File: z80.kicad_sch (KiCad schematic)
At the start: 46 parts, among them IC4 Z80CPU, IC5 LC3664, IC901 TL974

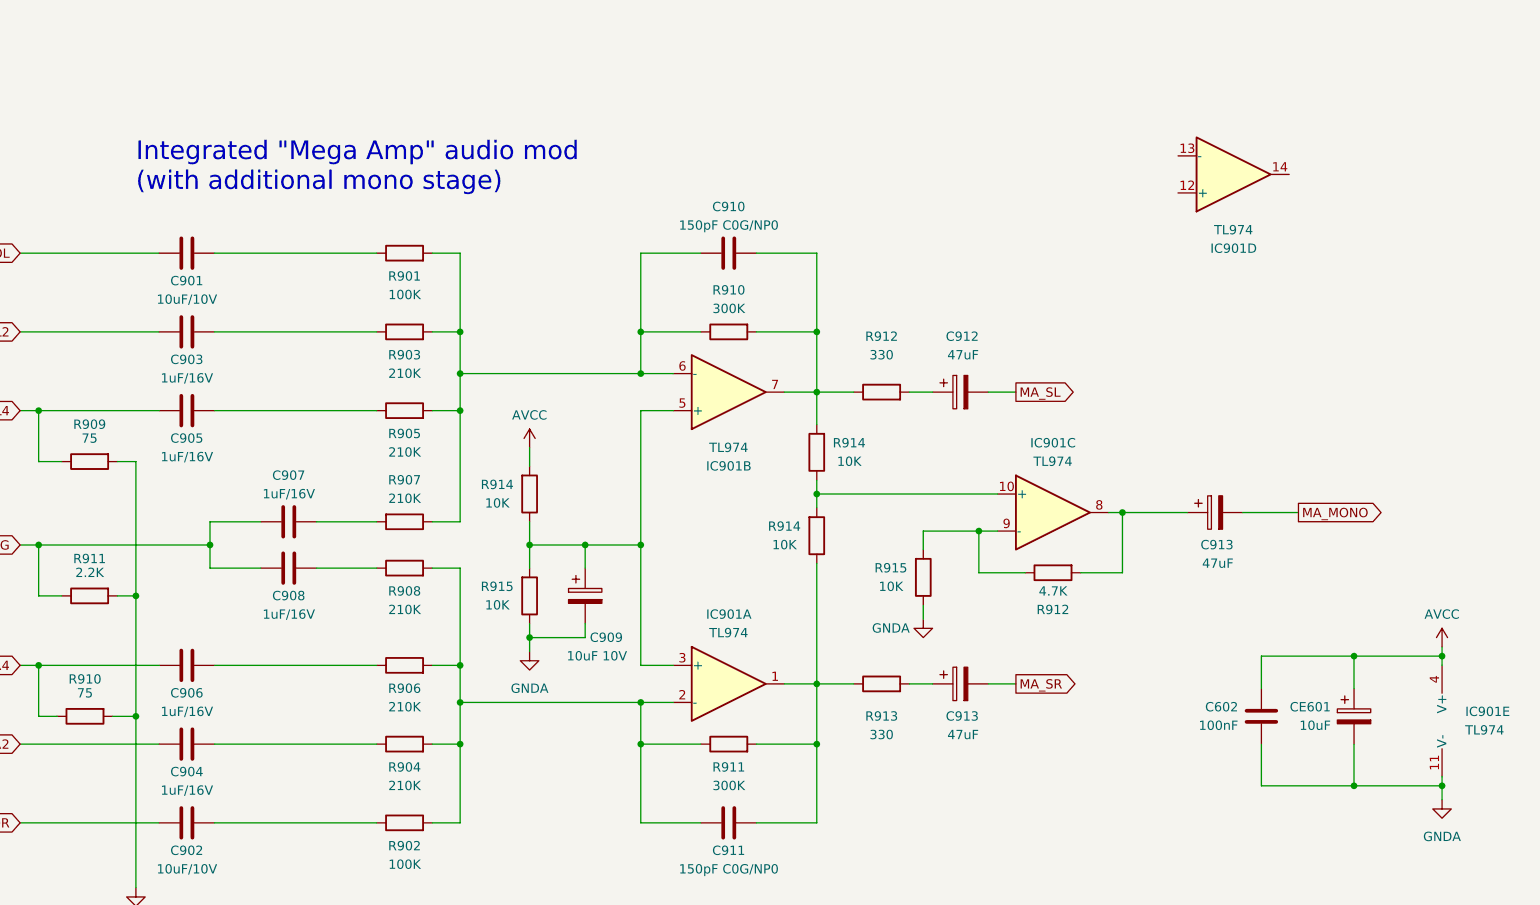
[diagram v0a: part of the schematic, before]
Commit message: Remove mono audio, switch to 2-unit opamp.
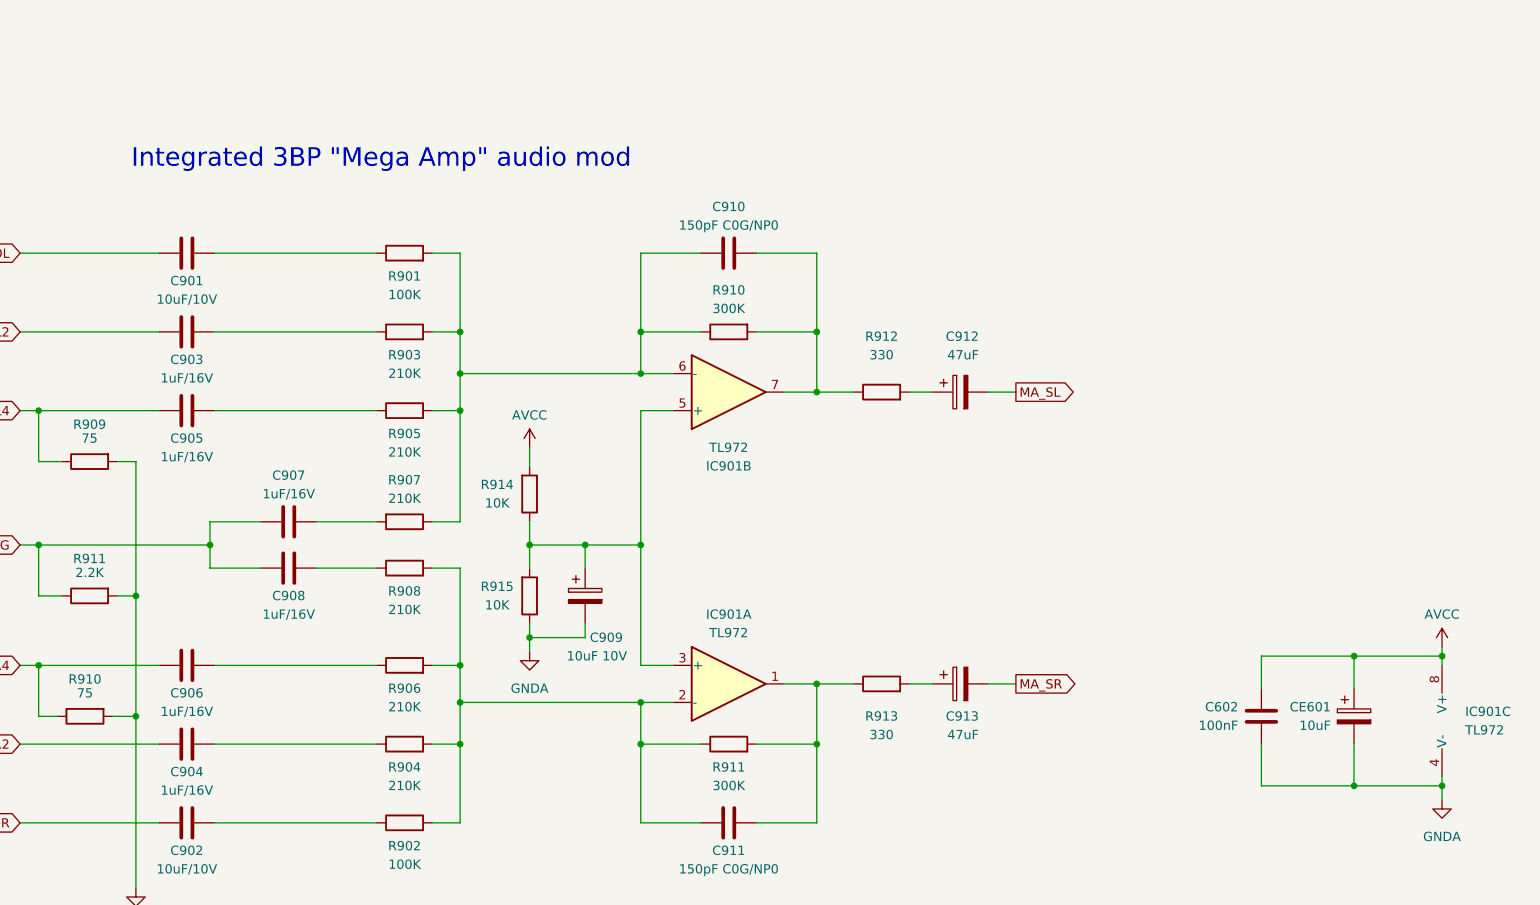
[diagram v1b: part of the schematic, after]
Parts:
- removed C913: 47uF, Capacitor_THT:CP_Radial_D5.0mm_P2.50mm, symbol Device:C_Polarized
- removed unit 4 of IC901
- removed unit 3 of IC901
- removed R912: 4.7K, Resistor_SMD:R_0805_2012Metric, symbol Device:R
- removed R914 (x2), R915: 10K, Resistor_SMD:R_0805_2012Metric, symbol Device:R
- IC901: value TL974 -> TL972; footprint Package_SO:SO-14_3.9x8.65mm_P1.27mm -> Package_SO:SO-8_3.9x4.9mm_P1.27mm; symbol Amplifier_Operational:TL064 -> Amplifier_Operational:TL062
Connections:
- net AVCC: now also IC901.8 (V+); no longer IC901.4 (V+)
- net GNDA: now also IC901.4 (V-); no longer IC901.11 (V-)
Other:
- note added: "Integrated 3BP "Mega Amp" audio mod"
- note removed: "Integrated "Mega Amp" audio mod (with additional mono stage)"

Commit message: Added LCSC Part # for some of the bird seed
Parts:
- C602: LCSC Part # (none) -> C2237864
- C901, C902: LCSC Part # (none) -> C2265547
- C903: LCSC Part # (none) -> C2224419
- C903, C904, C905, C906, C907, C908: LCSC Part # (none) -> C1850591
- C910, C911: LCSC Part # (none) -> C2230620
- R901, R902: LCSC Part # (none) -> C844935
- R903, R904, R905, R906, R907, R908: LCSC Part # (none) -> C2080690
- R909, R910: LCSC Part # (none) -> C313959
- R910, R911: LCSC Part # (none) -> C1881308
- R911: LCSC Part # (none) -> C3008897
- R912, R913: LCSC Part # (none) -> C844839
- R914, R915: LCSC Part # (none) -> C844937
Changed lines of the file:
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@@
+      (effects (font (size 1.27 1.27)) hide)
+    )
+    (property "LCSC Part #" "C1850591" (at 115.57 231.775 0)
       (effects (font (size 1.27 1.27)) hide)
     )
@@
       (effects (font (size 1.27 1.27)) hide)
     )
+    (property "LCSC Part #" "C2230620" (at 189.865 175.26 0)
+      (effects (font (size 1.27 1.27)) hide)
+    )
     (pin "1")
     (pin "2")
@@
       (effects (font (size 1.27 1.27)) hide)
     )
+    (property "LCSC Part #" "C2265547" (at 115.57 253.365 0)
+      (effects (font (size 1.27 1.27)) hide)
+    )
     (pin "1")
     (pin "2")
@@
     )
     (property "DigiKey" "P210KCCT-ND" (at 145.415 186.055 0)
+      (effects (font (size 1.27 1.27)) hide)
+    )
+    (property "LCSC Part #" "C2080690" (at 145.415 186.055 0)
       (effects (font (size 1.27 1.27)) hide)
     )
@@
     )
     (property "DigiKey" "493-13447-1-ND" (at 221.615 234.315 0)
+      (effects (font (size 1.27 1.27)) hide)
+    )
+    (property "LCSC Part #" "" (at 221.615 234.315 0)
       (effects (font (size 1.27 1.27)) hide)
     )
@@
     )
     (property "DigiKey" "296-21693-1-ND" (at 189.865 234.315 0)
+      (effects (font (size 1.27 1.27)) hide)
+    )
+    (property "LCSC Part #" "" (at 189.865 234.315 0)
       (effects (font (size 1.27 1.27)) hide)
     )
@@
       (effects (font (size 1.27 1.27)) hide)
     )
+    (property "LCSC Part #" "C2080690" (at 145.415 212.09 0)
+      (effects (font (size 1.27 1.27)) hide)
+    )
     (pin "1")
     (pin "2")
@@
       (effects (font (size 1.27 1.27)) hide)
     )
+    (property "LCSC Part #" "C313959" (at 101.6 238.76 0)
+      (effects (font (size 1.27 1.27)) hide)
+    )
     (pin "1")
     (pin "2")
@@
     )
     (property "DigiKey" "" (at 115.57 242.57 0)
+      (effects (font (size 1.27 1.27)) hide)
+    )
+    (property "LCSC Part #" "C1850591" (at 115.57 242.57 0)
       (effects (font (size 1.27 1.27)) hide)
     )
@@
       (effects (font (size 1.27 1.27)) hide)
     )
+    (property "LCSC Part #" "C2080690" (at 145.415 231.775 0)
+      (effects (font (size 1.27 1.27)) hide)
+    )
     (pin "1")
     (pin "2")
@@
     )
     (property "DigiKey" "P210KCCT-ND" (at 145.415 242.57 0)
+      (effects (font (size 1.27 1.27)) hide)
+    )
+    (property "LCSC Part #" "C2080690" (at 145.415 242.57 0)
       (effects (font (size 1.27 1.27)) hide)
     )
@@
       (effects (font (size 1.27 1.27)) hide)
     )
+    (property "LCSC Part #" "C2237864" (at 262.89 238.76 0)
+      (effects (font (size 1.27 1.27)) hide)
+    )
     (pin "1")
     (pin "2")
@@
     )
     (property "DigiKey" "" (at 145.415 175.26 0)
+      (effects (font (size 1.27 1.27)) hide)
+    )
+    (property "LCSC Part #" "C844935" (at 145.415 175.26 0)
       (effects (font (size 1.27 1.27)) hide)
     )
@@
       (effects (font (size 1.27 1.27)) hide)
     )
+    (property "LCSC Part #" "C313959" (at 52.07 175.26 0)
+      (effects (font (size 1.27 1.27)) hide)
+    )
     (pin "1")
     (pin "2")
@@
     )
     (property "DigiKey" "296-21693-1-ND" (at 189.865 194.31 0)
+      (effects (font (size 1.27 1.27)) hide)
+    )
+    (property "LCSC Part #" "" (at 189.865 194.31 0)
       (effects (font (size 1.27 1.27)) hide)
     )
@@
       (effects (font (size 1.27 1.27)) hide)
     )
+    (property "LCSC Part #" "" (at 80.772 33.782 0)
+      (effects (font (size 1.27 1.27)) hide)
+    )
     (pin "1")
     (pin "2")
@@
       (effects (font (size 1.27 1.27)) hide)
     )
+    (property "LCSC Part #" "C2080690" (at 145.415 218.44 0)
+      (effects (font (size 1.27 1.27)) hide)
+    )
     (pin "1")
     (pin "2")
@@
       (effects (font (size 1.27 1.27)) hide)
     )
+    (property "LCSC Part #" "C2224419" (at 167.64 33.655 0)
+      (effects (font (size 1.27 1.27)) hide)
+    )
     (pin "1")
     (pin "2")
@@
       (effects (font (size 1.27 1.27)) hide)
     )
+    (property "LCSC Part #" "C2265547" (at 115.57 175.26 0)
+      (effects (font (size 1.27 1.27)) hide)
+    )
     (pin "1")
     (pin "2")
@@
       (effects (font (size 1.27 1.27)) hide)
     )
+    (property "LCSC Part #" "C844937" (at 162.56 222.25 0)
+      (effects (font (size 1.27 1.27)) hide)
+    )
     (pin "1")
     (pin "2")
@@
       (effects (font (size 1.27 1.27)) hide)
     )
+    (property "LCSC Part #" "C1850591" (at 115.57 186.055 0)
+      (effects (font (size 1.27 1.27)) hide)
+    )
     (pin "1")
     (pin "2")
@@
       (effects (font (size 1.27 1.27)) hide)
     )
+    (property "LCSC Part #" "C2230620" (at 189.865 253.365 0)
+      (effects (font (size 1.27 1.27)) hide)
+    )
     (pin "1")
     (pin "2")
@@
       (effects (font (size 1.27 1.27)) hide)
     )
+    (property "LCSC Part #" "C1881308" (at 189.865 186.055 0)
+      (effects (font (size 1.27 1.27)) hide)
+    )
     (pin "1")
     (pin "2")
@@
       (effects (font (size 1.27 1.27)) hide)
     )
+    (property "LCSC Part #" "C844937" (at 162.56 208.28 0)
+      (effects (font (size 1.27 1.27)) hide)
+    )
     (pin "1")
     (pin "2")
@@
     )
     (property "DigiKey" "P75.0CCT-ND" (at 102.235 203.835 0)
+      (effects (font (size 1.27 1.27)) hide)
+    )
+    (property "LCSC Part #" "C313959" (at 102.235 203.835 0)
       (effects (font (size 1.27 1.27)) hide)
     )
@@
     )
     (property "DigiKey" "493-13447-1-ND" (at 221.615 194.31 0)
+      (effects (font (size 1.27 1.27)) hide)
+    )
+    (property "LCSC Part #" "" (at 221.615 194.31 0)
       (effects (font (size 1.27 1.27)) hide)
     )
@@
       (effects (font (size 1.27 1.27)) hide)
     )
+    (property "LCSC Part #" "" (at 170.18 222.25 0)
+      (effects (font (size 1.27 1.27)) hide)
+    )
     (pin "1")
     (pin "2")
@@
       (effects (font (size 1.27 1.27)) hide)
     )
+    (property "LCSC Part #" "C1850591" (at 129.54 218.44 0)
+      (effects (font (size 1.27 1.27)) hide)
+    )
     (pin "1")
     (pin "2")
@@
       (effects (font (size 1.27 1.27)) hide)
     )
+    (property "LCSC Part #" "C2080690" (at 145.415 196.85 0)
+      (effects (font (size 1.27 1.27)) hide)
+    )
     (pin "1")
     (pin "2")
@@
     )
     (property "DigiKey" "P2.20KCCT-ND" (at 102.235 222.25 0)
+      (effects (font (size 1.27 1.27)) hide)
+    )
+    (property "LCSC Part #" "C3008897" (at 102.235 222.25 0)
       (effects (font (size 1.27 1.27)) hide)
     )
@@
       (effects (font (size 1.27 1.27)) hide)
     )
+    (property "LCSC Part #" "" (at 275.59 238.76 0)
+      (effects (font (size 1.27 1.27)) hide)
+    )
     (pin "1")
     (pin "2")
@@
       (effects (font (size 1.27 1.27)) hide)
     )
+    (property "LCSC Part #" "C2224419" (at 93.472 33.782 0)
+      (effects (font (size 1.27 1.27)) hide)
+    )
     (pin "1")
     (pin "2")
@@
     )
     (property "DigiKey" "" (at 145.415 253.365 0)
+      (effects (font (size 1.27 1.27)) hide)
+    )
+    (property "LCSC Part #" "C844935" (at 145.415 253.365 0)
       (effects (font (size 1.27 1.27)) hide)
     )
@@
     )
     (property "DigiKey" "" (at 210.82 234.315 0)
+      (effects (font (size 1.27 1.27)) hide)
+    )
+    (property "LCSC Part #" "C844839" (at 210.82 234.315 0)
       (effects (font (size 1.27 1.27)) hide)
     )
@@
     )
     (property "DigiKey" "" (at 74.93 83.185 0)
+      (effects (font (size 1.27 1.27)) hide)
+    )
+    (property "LCSC Part #" "" (at 74.93 83.185 0)
       (effects (font (size 1.27 1.27)) hide)
     )
@@
       (effects (font (size 1.27 1.27)) hide)
     )
+    (property "LCSC Part #" "" (at 290.195 239.395 0)
+      (effects (font (size 1.27 1.27)) hide)
+    )
     (pin "1")
     (pin "2")
@@
       (effects (font (size 1.27 1.27)) hide)
     )
+    (property "LCSC Part #" "C1881308" (at 189.865 242.57 0)
+      (effects (font (size 1.27 1.27)) hide)
+    )
     (pin "1")
     (pin "2")
@@
     )
     (property "DigiKey" "" (at 129.54 212.09 0)
+      (effects (font (size 1.27 1.27)) hide)
+    )
+    (property "LCSC Part #" "C1850591" (at 129.54 212.09 0)
       (effects (font (size 1.27 1.27)) hide)
     )
@@
     )
     (property "DigiKey" "" (at 210.82 194.31 0)
+      (effects (font (size 1.27 1.27)) hide)
+    )
+    (property "LCSC Part #" "C844839" (at 210.82 194.31 0)
       (effects (font (size 1.27 1.27)) hide)
     )
@@
     )
     (property "DigiKey" "" (at 158.75 80.645 0)
+      (effects (font (size 1.27 1.27)) hide)
+    )
+    (property "LCSC Part #" "" (at 158.75 80.645 0)
       (effects (font (size 1.27 1.27)) hide)
     )
@@
       (effects (font (size 1.27 1.27)) hide)
     )
+    (property "LCSC Part #" "C313959" (at 52.07 191.135 0)
+      (effects (font (size 1.27 1.27)) hide)
+    )
     (pin "1")
     (pin "2")
@@
     )
     (property "DigiKey" "" (at 219.71 109.22 0)
+      (effects (font (size 1.27 1.27)) hide)
+    )
+    (property "LCSC Part #" "" (at 219.71 109.22 0)
       (effects (font (size 1.27 1.27)) hide)
     )
@@
       (effects (font (size 1.27 1.27)) hide)
     )
+    (property "LCSC Part #" "C1850591" (at 115.57 196.85 0)
+      (effects (font (size 1.27 1.27)) hide)
+    )

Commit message: Added more JLC Part numbers
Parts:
- IC901: LCSC Part # (none) -> C46127
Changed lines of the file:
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@@
       (effects (font (size 1.27 1.27)) hide)
     )
-    (property "LCSC Part #" "" (at 189.865 234.315 0)
+    (property "LCSC Part #" "C46127" (at 189.865 234.315 0)
       (effects (font (size 1.27 1.27)) hide)
     )
@@
       (effects (font (size 1.27 1.27)) hide)
     )
-    (property "LCSC Part #" "" (at 189.865 194.31 0)
+    (property "LCSC Part #" "C46127" (at 189.865 194.31 0)
       (effects (font (size 1.27 1.27)) hide)
     )
@@
       (effects (font (size 1.27 1.27)) hide)
     )
-    (property "LCSC Part #" "" (at 290.195 239.395 0)
-      (effects (font (size 1.27 1.27)) hide)
-    )
+    (property "LCSC Part #" "C46127" (at 290.195 239.395 0)
+      (effects (font (size 1.27 1.27)) hide)
+    )
